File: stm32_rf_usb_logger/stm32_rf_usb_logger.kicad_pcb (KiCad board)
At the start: 4 copper layers, 42.6 x 16.5 mm, 38 parts, among them J1 SWD, J2 USB_B_Micro, J3 Conn_Coaxial, U1 XC6206PxxxMR, U2 STM32L432KBUx, U3 USBLC6-2SC6, U4 nRF24L01P, Y2 16MHz

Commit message: deleted layout for testing
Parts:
- removed C1, C2: 10u, Capacitor_SMD:C_0603_1608Metric_Pad1.08x0.95mm_HandSolder
- removed C10, C11, C3, C4, C5, C7, C9: 100n, Capacitor_SMD:C_0402_1005Metric
- removed C12: 33n, Capacitor_SMD:C_0402_1005Metric
- removed C13: 1p5, Capacitor_SMD:C_0402_1005Metric
- removed C14: 1p, Capacitor_SMD:C_0402_1005Metric
- removed C15: 4p7, Capacitor_SMD:C_0402_1005Metric
- removed C16: 2n2, Capacitor_SMD:C_0402_1005Metric
- removed C17, C18: 12p, Capacitor_SMD:C_0402_1005Metric
- removed C6, C8: 1U, Capacitor_SMD:C_0402_1005Metric
- removed D1: GR, LED_SMD:LED_0402_1005Metric
- removed D2: YE, LED_SMD:LED_0402_1005Metric
- removed F1: 1000mA, Fuse:Fuse_0603_1608Metric_Pad1.05x0.95mm_HandSolder
- removed FB1: 100 @ 100MHz, Inductor_SMD:L_0805_2012Metric
- removed J1: SWD, Connector_PinHeader_2.54mm:PinHeader_2x05_P2.54mm_Vertical
- removed J2: USB_B_Micro, Connector_USB:USB_Micro-B_Molex-105017-0001
- removed J3: Conn_Coaxial, Connector_Coaxial:SMA_Samtec_SMA-J-P-X-ST-EM1_EdgeMount
- removed L1: 3n9, Inductor_SMD:L_0402_1005Metric
- removed L2: 8n2, Inductor_SMD:L_0402_1005Metric
- removed L3: 2n7, Inductor_SMD:L_0402_1005Metric
- removed R1: 10k, Resistor_SMD:R_0402_1005Metric
- removed R2, R3: 220, Resistor_SMD:R_0603_1608Metric
- removed R4: 22k, Resistor_SMD:R_0603_1608Metric
- removed R5: 1M, Resistor_SMD:R_0402_1005Metric_Pad0.72x0.64mm_HandSolder
- removed U1: XC6206PxxxMR, Package_TO_SOT_SMD:SOT-23-3
- removed U2: STM32L432KBUx, Package_DFN_QFN:QFN-32-1EP_5x5mm_P0.5mm_EP3.45x3.45mm
- removed U3: USBLC6-2SC6, Package_TO_SOT_SMD:SOT-23-6
- removed U4: nRF24L01P, Package_DFN_QFN:QFN-20-1EP_4x4mm_P0.5mm_EP2.5x2.5mm
- removed Y2: 16MHz, Crystal:Crystal_SMD_3225-4Pin_3.2x2.5mm
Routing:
- net GND: track 53.3 -> 0.00 mm, vias 50 -> 0
- net +3.3V: track 33.7 -> 0.00 mm, vias 18 -> 0
- net Net-(D2-A): track 13.5 -> 0.00 mm, vias 2 -> 0
- net NRF_XC2: track 12.3 -> 0.00 mm
- net +5V: track 12.2 -> 0.00 mm, vias 2 -> 0
- net NRST: track 11.8 -> 0.00 mm, vias 1 -> 0
- net USB_D-: track 11.3 -> 0.00 mm
- net USB_D+: track 11.2 -> 0.00 mm
- net SWDIO: track 9.59 -> 0.00 mm, vias 1 -> 0
- net Net-(D1-A): track 9.00 -> 0.00 mm, vias 2 -> 0
- net NRF_XC1: track 8.63 -> 0.00 mm
- net SWCLK: track 8.09 -> 0.00 mm, vias 1 -> 0
- net NRF_VDD_PA: track 6.87 -> 0.00 mm
- net SPI3_SCK: track 6.49 -> 0.00 mm, vias 2 -> 0
- net NRF_IRQ: track 6.37 -> 0.00 mm, vias 2 -> 0
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- removed copper zone on F.Cu, net (none)
- removed copper zone on F.Cu, net +3.3V
- removed copper zone on In2.Cu, net +3.3V
- removed copper zone on F.Cu, net +5V
- removed copper zone on F.Cu, net /regIn
- removed copper zone on B.Cu, net GND
- removed copper zone on F.Cu, net GND
- removed copper zone on In1.Cu, net GND
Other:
- board outline removed
- board text removed: "SWD"

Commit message: completed layout
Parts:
- added C1: 10u, Capacitor_SMD:C_0603_1608Metric_Pad1.08x0.95mm_HandSolder, F.Cu at (127.1, 93.9)
- added C10: 100n, Capacitor_SMD:C_0402_1005Metric, F.Cu at (153.1, 96.7)
- added C11: 100n, Capacitor_SMD:C_0402_1005Metric, F.Cu at (149.9, 94.8)
- added C12: 1p, Capacitor_SMD:C_0402_1005Metric, F.Cu at (161.4, 97.9)
- added C13: 2n2, Capacitor_SMD:C_0402_1005Metric, F.Cu at (158.6, 101.3)
- added C14: 4p7, Capacitor_SMD:C_0402_1005Metric, F.Cu at (158.7, 102.6)
- added C15: 100n, Capacitor_SMD:C_0402_1005Metric, F.Cu at (126.1, 101.6)
- added C16: 33n, Capacitor_SMD:C_0402_1005Metric, F.Cu at (148.9, 94.8)
- added C17: 12p, Capacitor_SMD:C_0402_1005Metric, F.Cu at (146.2, 106.5)
- added C18: 12p, Capacitor_SMD:C_0402_1005Metric, F.Cu at (152.4, 106.7)
- added C2: 10u, Capacitor_SMD:C_0603_1608Metric_Pad1.08x0.95mm_HandSolder, F.Cu at (133.6, 94.2)
- added C3: 1U, Capacitor_SMD:C_0402_1005Metric, F.Cu at (136.0, 98.0)
- added C4: 100n, Capacitor_SMD:C_0402_1005Metric, F.Cu at (142.6, 94.2)
- added C5: 100n, Capacitor_SMD:C_0402_1005Metric, F.Cu at (137.1, 100.7)
- added C6: 100n, Capacitor_SMD:C_0402_1005Metric, F.Cu at (140.6, 94.2)
- added C7: 1p5, Capacitor_SMD:C_0402_1005Metric, F.Cu at (159.2, 98.1)
- added C8: 1U, Capacitor_SMD:C_0402_1005Metric, F.Cu at (147.6, 94.9)
- added C9: 100n, Capacitor_SMD:C_0402_1005Metric, F.Cu at (147.9, 101.9)
- added D1: GR, LED_SMD:LED_0402_1005Metric, F.Cu at (135.6, 93.3)
- added D2: YE, LED_SMD:LED_0402_1005Metric, F.Cu at (136.7, 93.3)
- added F1: 1000mA, Fuse:Fuse_0603_1608Metric_Pad1.05x0.95mm_HandSolder, F.Cu at (120.1, 93.1)
- added FB1: 100 @ 100MHz, Inductor_SMD:L_0805_2012Metric, F.Cu at (124.1, 93.2)
- added J1: USB_B_Micro, Connector_USB:USB_Micro-B_Molex-105017-0001, F.Cu at (120.0, 99.8)
- added J2: Conn_Coaxial, Connector_Coaxial:SMA_Samtec_SMA-J-P-X-ST-EM1_EdgeMount, F.Cu at (164.7, 99.8)
- added J3: SWD, Connector_PinHeader_2.54mm:PinHeader_2x05_P2.54mm_Vertical, F.Cu at (135.0, 104.0)
- added Je: RFShield_OnePiece, RF_Shielding:Laird_Technologies_BMI-S-102_16.50x16.50mm, F.Cu at (160.6, 100.4)
- added L1: 3n9, Inductor_SMD:L_0402_1005Metric, F.Cu at (157.1, 98.2)
- added L2: 8n2, Inductor_SMD:L_0402_1005Metric, F.Cu at (155.5, 98.6)
- added L3: 2n7, Inductor_SMD:L_0402_1005Metric, F.Cu at (156.6, 100.6)
- added R1: 10k, Resistor_SMD:R_0402_1005Metric, F.Cu at (144.9, 96.5)
- added R2: 220, Resistor_SMD:R_0603_1608Metric, F.Cu at (135.8, 96.0)
- added R3: 220, Resistor_SMD:R_0603_1608Metric, F.Cu at (139.2, 93.8)
- added R4: 22k, Resistor_SMD:R_0603_1608Metric, F.Cu at (151.6, 94.3)
- added R5: 1M, Resistor_SMD:R_0402_1005Metric_Pad0.72x0.64mm_HandSolder, F.Cu at (150.4, 104.0)
- added U1: XC6206PxxxMR, Package_TO_SOT_SMD:SOT-23-3, F.Cu at (130.5, 94.2)
- added U2: USBLC6-2SC6, Package_TO_SOT_SMD:SOT-23-6, F.Cu at (130.6, 99.4)
- added U3: STM32L432KBUx, Package_DFN_QFN:QFN-32-1EP_5x5mm_P0.5mm_EP3.45x3.45mm, F.Cu at (140.8, 98.5)
- added U4: nRF24L01P, Package_DFN_QFN:QFN-20-1EP_4x4mm_P0.5mm_EP2.5x2.5mm, F.Cu at (149.8, 98.5)
- added Y1: 16MHz, Crystal:Crystal_SMD_3225-4Pin_3.2x2.5mm, F.Cu at (149.3, 106.4)
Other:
- board outline added: 49.3 x 17.3 mm

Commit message: Done
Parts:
- moved C5 1.25 mm to (137.2, 99.4)
- moved R4 1.05 mm to (152.5, 94.7), turned to 180 degrees
- moved C4 0.63 mm to (143.2, 94.2)
- moved R5 0.47 mm to (150.3, 104.5)
- moved Y1 0.47 mm to (149.3, 106.9)
- moved C9 0.36 mm to (147.7, 101.6)
- moved C18 0.36 mm to (152.0, 106.7)
- moved C17 0.36 mm to (146.5, 106.7)
- moved C10 0.27 mm to (153.0, 97.0), turned to -90 degrees
- renumbered Je to e
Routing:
- net GND: track 0.00 -> 52.1 mm, vias 0 -> 59
- net NRST: track 0.00 -> 33.8 mm, vias 0 -> 1
- net +3.3V: track 0.00 -> 28.1 mm, vias 0 -> 14
- net SWCLK: track 0.00 -> 15.1 mm
- net USB_D-: track 0.00 -> 13.0 mm
- net USB_D+: track 0.00 -> 12.3 mm
- net NRF_XC1: track 0.00 -> 12.3 mm, vias 0 -> 2
- net USB_CONN_D-: track 0.00 -> 10.5 mm
- net SWDIO: track 0.00 -> 10.4 mm
- net +5V: track 0.00 -> 10.1 mm, vias 0 -> 5
- net USB_CONN_D+: track 0.00 -> 9.72 mm
- net NRF_VDD_PA: track 0.00 -> 8.38 mm
- net NRF_XC2: track 0.00 -> 8.04 mm
- net Net-(J2-In): track 0.00 -> 6.05 mm
- net NRF_IRQ: track 0.00 -> 6.02 mm
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- added copper zone on F.Cu, net +3.3V
- added copper zone on In2.Cu, net +3.3V
- added copper zone on In2.Cu, net +5V
- added copper zone on F.Cu, net GND
- added copper zone on In1.Cu, net GND
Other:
- board text added: "."
- board text added: "RX"
- board text added: "SWD"
- board text added: "TX"
- board text added: "Tam Anderson"
- board text added: "ULOGGER"

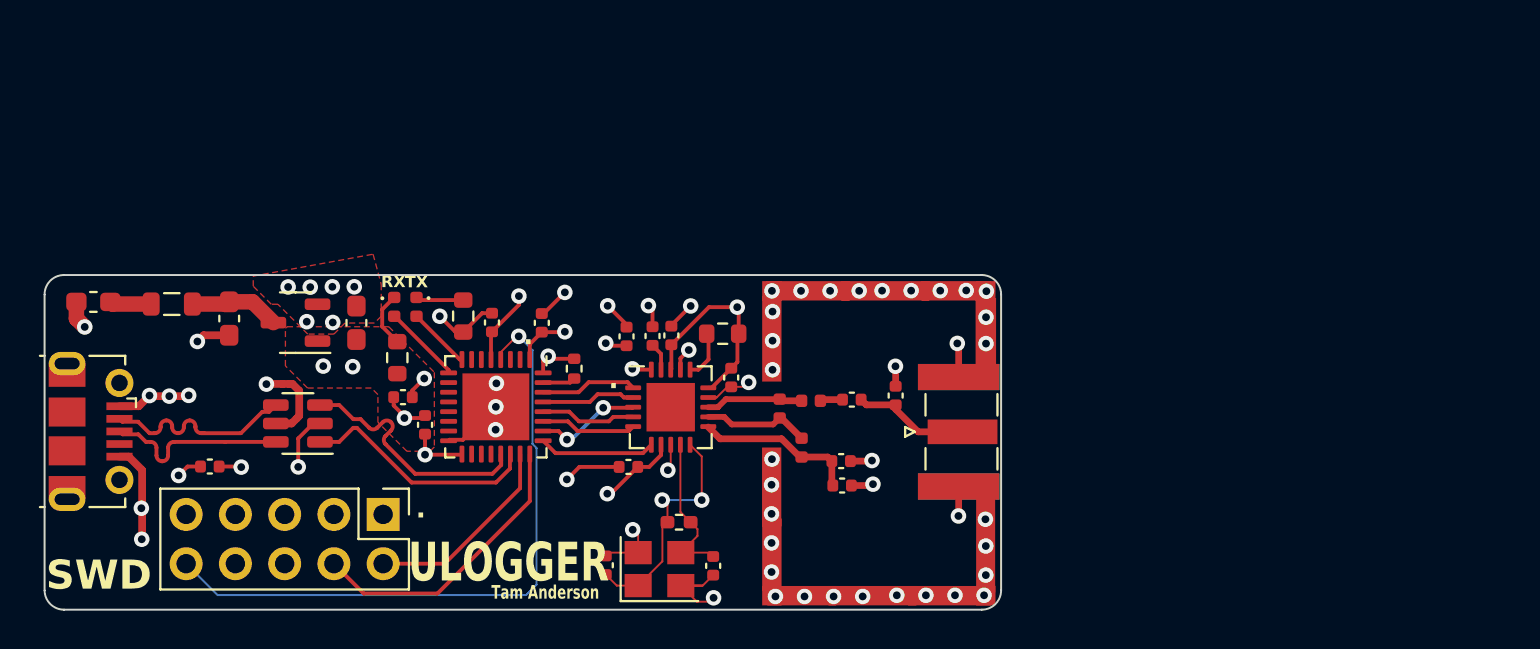
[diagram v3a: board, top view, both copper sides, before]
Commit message: optimised grounding
moved vias closer to pads
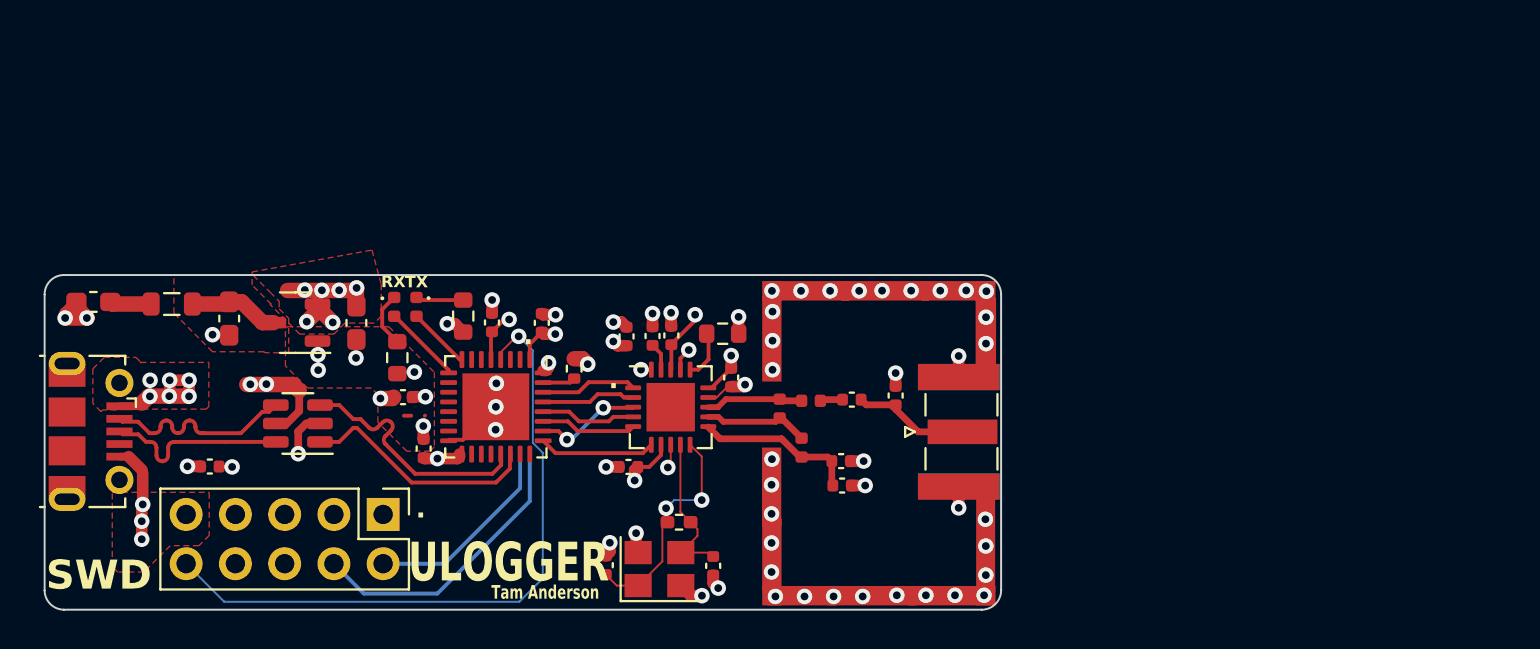
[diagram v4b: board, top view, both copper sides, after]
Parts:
- moved C5 1.22 mm to (137.1, 100.7)
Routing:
- net GND: track 52.1 -> 38.1 mm, vias 59 -> 67
- net +5V: track 10.1 -> 19.3 mm, vias 5 -> 10
- net +3.3V: track 28.1 -> 25.3 mm, vias 14 -> 16
- net NRST: track 33.8 -> 34.3 mm
- net NRF_XC1: track 12.3 -> 11.8 mm
- added copper zone on F.Cu, net +5V
- added copper zone on F.Cu, net /regIn
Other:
- board text added: "REV2"
